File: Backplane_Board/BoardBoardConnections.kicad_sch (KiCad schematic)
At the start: 30 parts, among them J25 Conn_01x03_Pin, J26 Conn_01x03_Pin, J27 Conn_01x03_Pin, J28 BM03B-SRSS-TB, J29 Conn_01x04, J30 Conn_01x05_Socket, J31 BM03B-SRSS-TB, J32 Conn_01x03_Pin, J33 Conn_01x03_Pin, J34 Conn_01x03_Pin, Q3 SI7615ADN-T1-GE3, U6 Pico

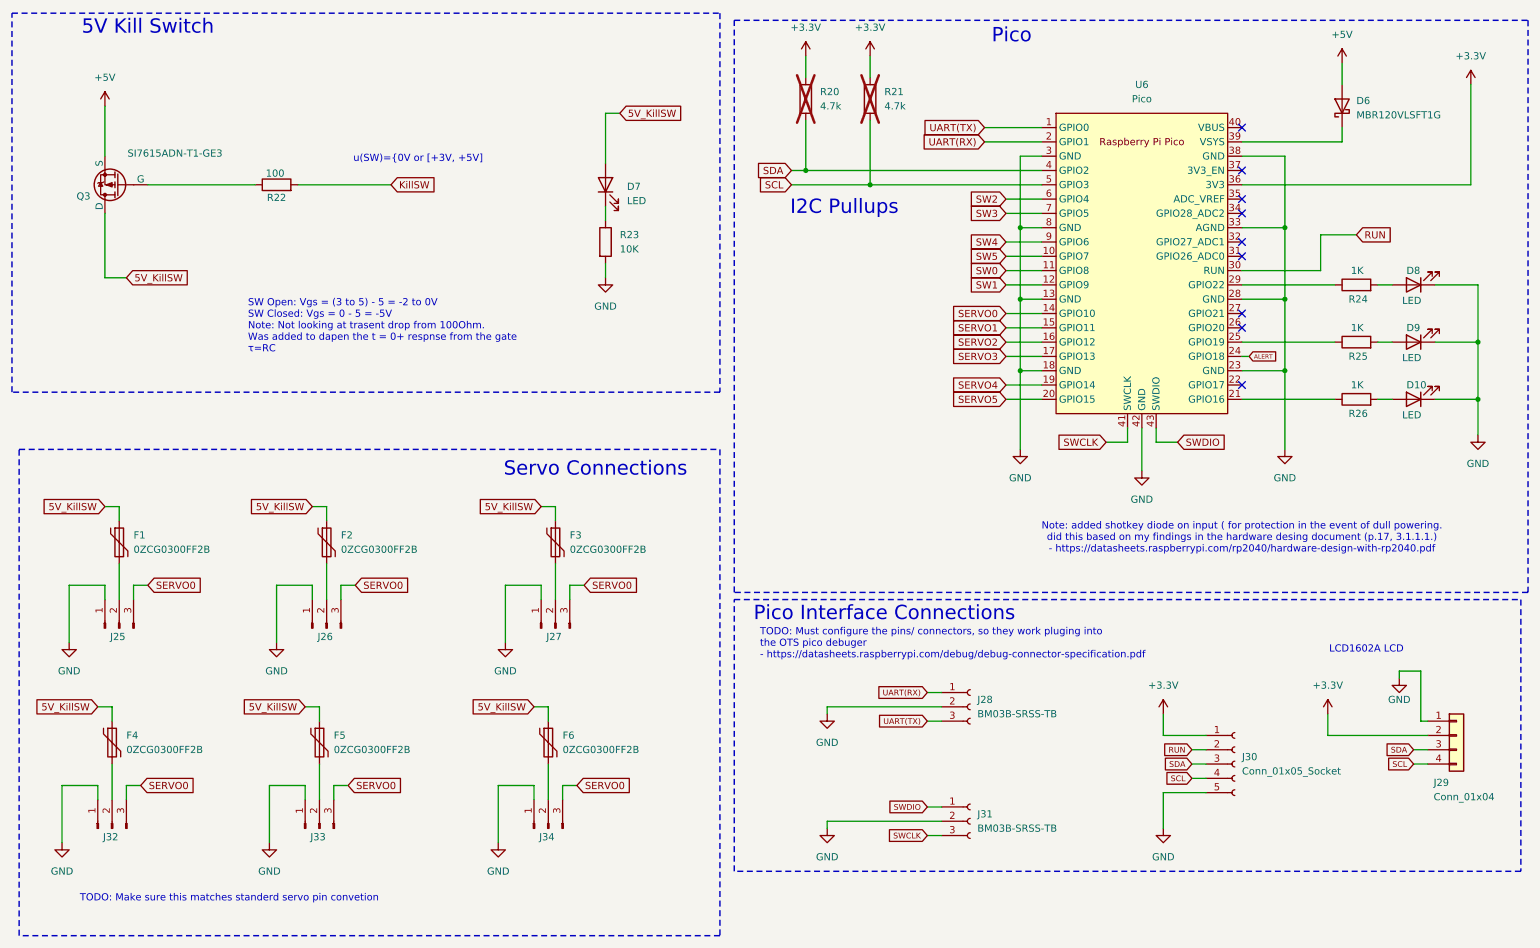
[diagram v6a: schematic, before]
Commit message: adding more footprints
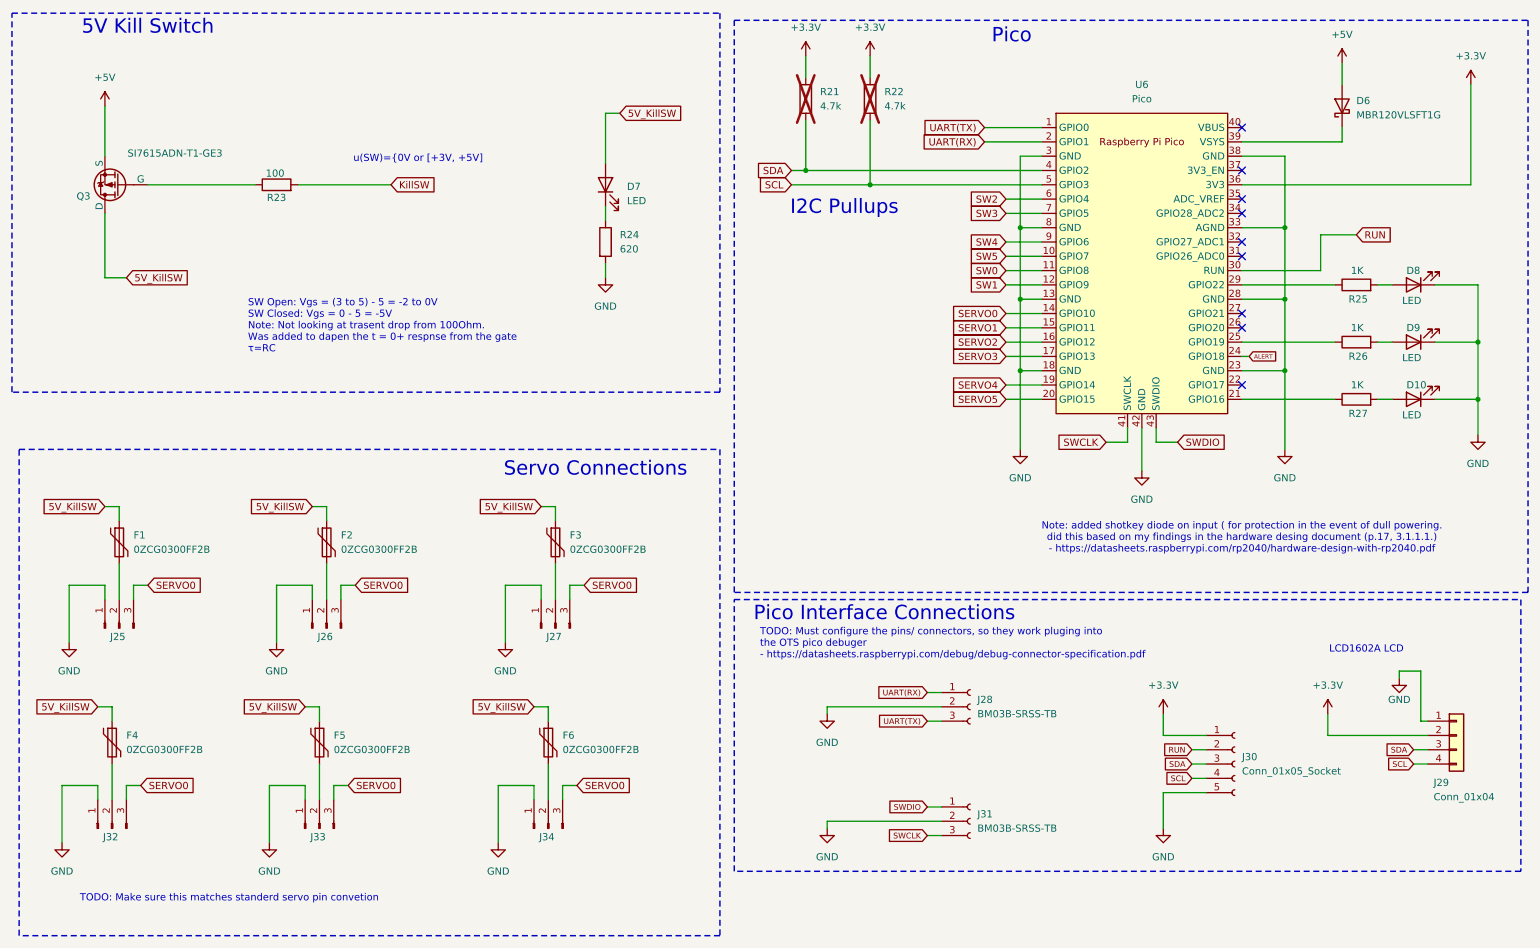
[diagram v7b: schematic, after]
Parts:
- D10, D7, D8, D9: footprint (none) -> LED_SMD:LED_0603_1608Metric
- D6: footprint (none) -> Diode_SMD:D_SOD-123F
- J25, J26, J27, J32, J33, J34: footprint (none) -> TerminalBlock:TerminalBlock_Xinya_XY308-2.54-3P_1x03_P2.54mm_Horizontal
- J29: footprint (none) -> Connector_PinSocket_1.00mm:PinSocket_1x04_P1.00mm_Vertical
- J30: footprint (none) -> Connector_PinHeader_1.00mm:PinHeader_1x05_P1.00mm_Vertical
- R21: renamed from R20; footprint (none) -> Resistor_SMD:R_1206_3216Metric_Pad1.30x1.75mm_HandSolder
- R22: renamed from R21; footprint (none) -> Resistor_SMD:R_1206_3216Metric_Pad1.30x1.75mm_HandSolder
- R23: renamed from R22; footprint (none) -> Resistor_SMD:R_1206_3216Metric_Pad1.30x1.75mm_HandSolder
- R24: renamed from R23; value 10K -> 620; footprint (none) -> Resistor_SMD:R_1206_3216Metric_Pad1.30x1.75mm_HandSolder
- R25: renamed from R24; footprint (none) -> Inductor_SMD:L_1206_3216Metric
- R26: renamed from R25; footprint (none) -> Inductor_SMD:L_1206_3216Metric
- R27: renamed from R26; footprint (none) -> Inductor_SMD:L_1206_3216Metric

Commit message: derat nest ifcation
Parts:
- added JP5: SolderJumper_2_Bridged, Jumper:SolderJumper-2_P1.3mm_Bridged_RoundedPad1.0x1.5mm, symbol Jumper:SolderJumper_2_Bridged
- added R46: 1k, Resistor_SMD:R_0805_2012Metric_Pad1.20x1.40mm_HandSolder, symbol Device:R
- J27: renamed from J25; footprint TerminalBlock:TerminalBlock_Xinya_XY308-2.54-3P_1x03_P2.54mm_Horizontal -> Connector_PinHeader_2.54mm:PinHeader_1x03_P2.54mm_Vertical
- J28: renamed from J26; footprint TerminalBlock:TerminalBlock_Xinya_XY308-2.54-3P_1x03_P2.54mm_Horizontal -> Connector_PinHeader_2.54mm:PinHeader_1x03_P2.54mm_Vertical
- J29: renamed from J27; footprint TerminalBlock:TerminalBlock_Xinya_XY308-2.54-3P_1x03_P2.54mm_Horizontal -> Connector_PinHeader_2.54mm:PinHeader_1x03_P2.54mm_Vertical
- J31: renamed from J29; footprint Connector_PinSocket_1.00mm:PinSocket_1x04_P1.00mm_Vertical -> Connector_Molex:Molex_PicoBlade_53047-0410_1x04_P1.25mm_Vertical
- J32: renamed from J30; footprint Connector_PinHeader_1.00mm:PinHeader_1x05_P1.00mm_Vertical -> Connector_PinSocket_2.54mm:PinSocket_1x05_P2.54mm_Vertical
- J34: renamed from J32; value Conn_01x03_Pin -> Connector_PinHeader_2.54mm:PinHeader_1x03_P2.54mm_Vertical; footprint TerminalBlock:TerminalBlock_Xinya_XY308-2.54-3P_1x03_P2.54mm_Horizontal -> Connector_PinHeader_2.54mm:PinHeader_1x03_P2.54mm_Vertical
- J35: renamed from J33; value Conn_01x03_Pin -> Connector_PinHeader_2.54mm:PinHeader_1x03_P2.54mm_Vertical; footprint TerminalBlock:TerminalBlock_Xinya_XY308-2.54-3P_1x03_P2.54mm_Horizontal -> Connector_PinHeader_2.54mm:PinHeader_1x03_P2.54mm_Vertical
- J36: renamed from J34; footprint TerminalBlock:TerminalBlock_Xinya_XY308-2.54-3P_1x03_P2.54mm_Horizontal -> Connector_PinHeader_2.54mm:PinHeader_1x03_P2.54mm_Vertical
- R23, R24: footprint Resistor_SMD:R_1206_3216Metric_Pad1.30x1.75mm_HandSolder -> Resistor_SMD:R_0805_2012Metric_Pad1.20x1.40mm_HandSolder
- R25, R26, R27: footprint Inductor_SMD:L_1206_3216Metric -> Resistor_SMD:R_0805_2012Metric_Pad1.20x1.40mm_HandSolder
- renumbered J28 to J30, J31 to J33
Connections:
- net +5V: now also R46.2
- net KillSW: now also JP5.2 (B)
- net at R27.1: now also D10.2 (A); no longer U6.21 (GPIO16)
- net at R27.2: now also U6.21 (GPIO16); no longer D10.2 (A)
- net esc_status: now reaches U6.26 (GPIO20)
- net esc_status: now also JP5.1 (A)
- net at Q3.2 (G), R23.1: now also R46.1
- no-connect marks 9 -> 8
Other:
- moved on the sheet: R27
